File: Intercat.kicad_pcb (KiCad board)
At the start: 2 copper layers, 72 parts, among them U1 CP2615-xx-xM, U10 MAX3250, U11 TLP185, U12 TLP185, U2 USBLC6-2SC6, U3 PCM3060, U4 MCP6002, U5 MCP6002, U6 MCP6002, U8 TLP185, U9 TLP185

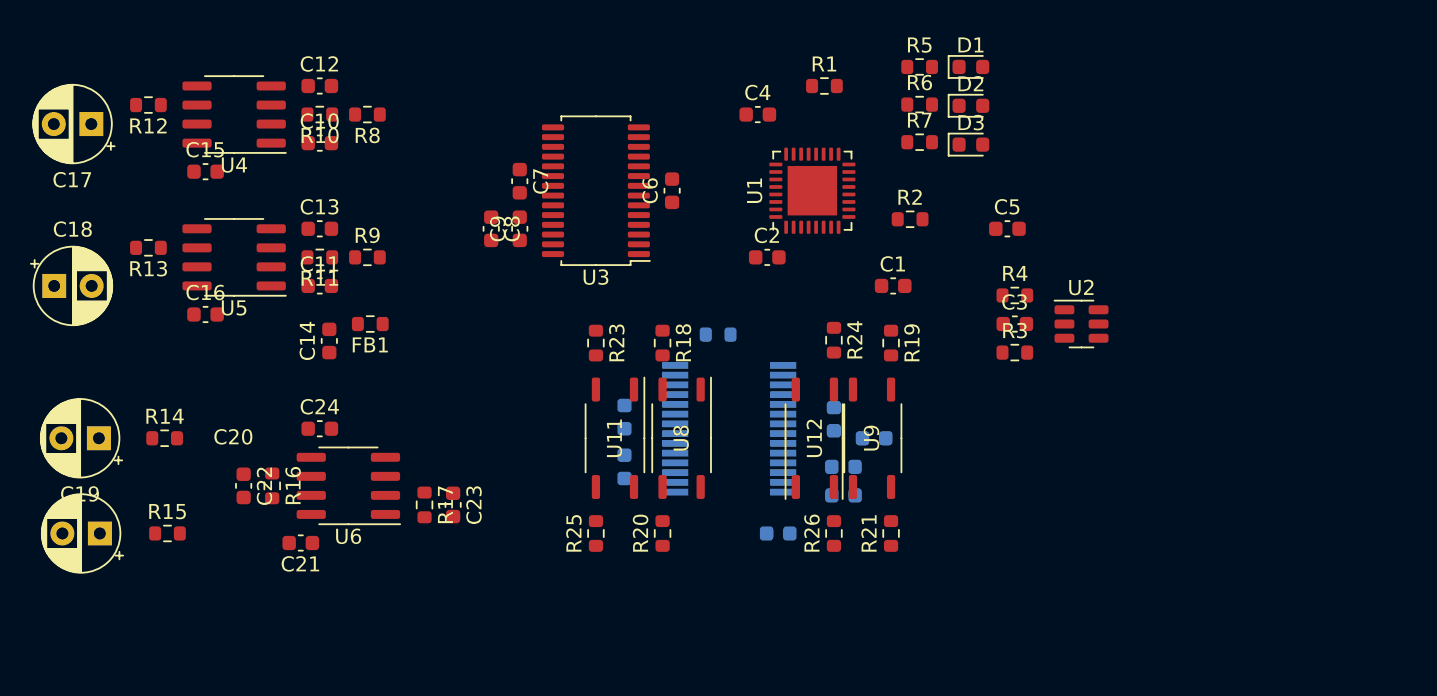
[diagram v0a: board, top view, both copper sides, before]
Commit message: Corrected audio Jacks
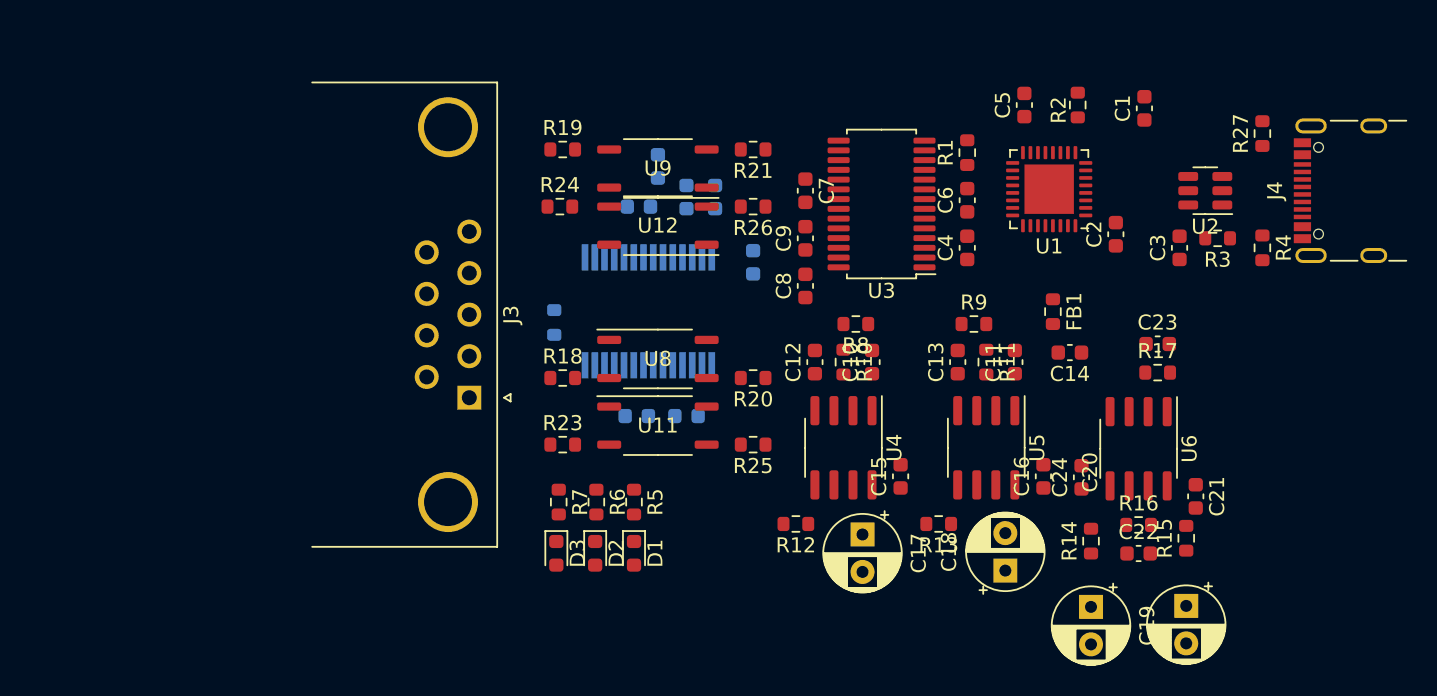
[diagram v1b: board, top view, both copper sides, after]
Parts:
- added J3: DE9_Receptacle, Connector_Dsub:DSUB-9_Female_Horizontal_P2.77x2.84mm_EdgePinOffset7.70mm_Housed_MountingHolesOffset9.12mm, F.Cu at (56.3, 93.2)
- added J4: USB_C_Receptacle_USB2.0, Connector_USB:USB_C_Receptacle_GCT_USB4105-xx-A_16P_TopMnt_Horizontal, F.Cu at (115.6, 79.4)
- added R27: 5k1, Resistor_SMD:R_0603_1608Metric, F.Cu at (109.2, 75.6)
- moved C20 72.6 mm to (104.1, 107.1), turned to -90 degrees
- moved R15 67.9 mm to (104.1, 102.6), turned to 90 degrees
- moved C19 67.1 mm to (97.8, 107.1), turned to -90 degrees
- moved C18 66.2 mm to (92.1, 104.7), turned to 90 degrees
- moved R14 62.2 mm to (97.8, 102.7), turned to 90 degrees
- moved C22 59.9 mm to (101.0, 103.6), turned to 0 degrees
- moved C21 59.8 mm to (104.8, 99.8), turned to -90 degrees
- moved C17 58.3 mm to (82.5, 102.3), turned to -90 degrees
- moved R16 57.8 mm to (101.0, 101.7), turned to 0 degrees
- moved C16 56.9 mm to (94.6, 98.4), turned to 90 degrees
- moved R13 55.8 mm to (87.6, 101.6)
- moved U6 52.8 mm to (101.0, 96.6), turned to -90 degrees
- moved U5 51.7 mm to (90.8, 96.5), turned to -90 degrees
- moved R12 51.4 mm to (78.1, 101.6)
- moved C24 50.9 mm to (97.2, 98.5), turned to 90 degrees
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
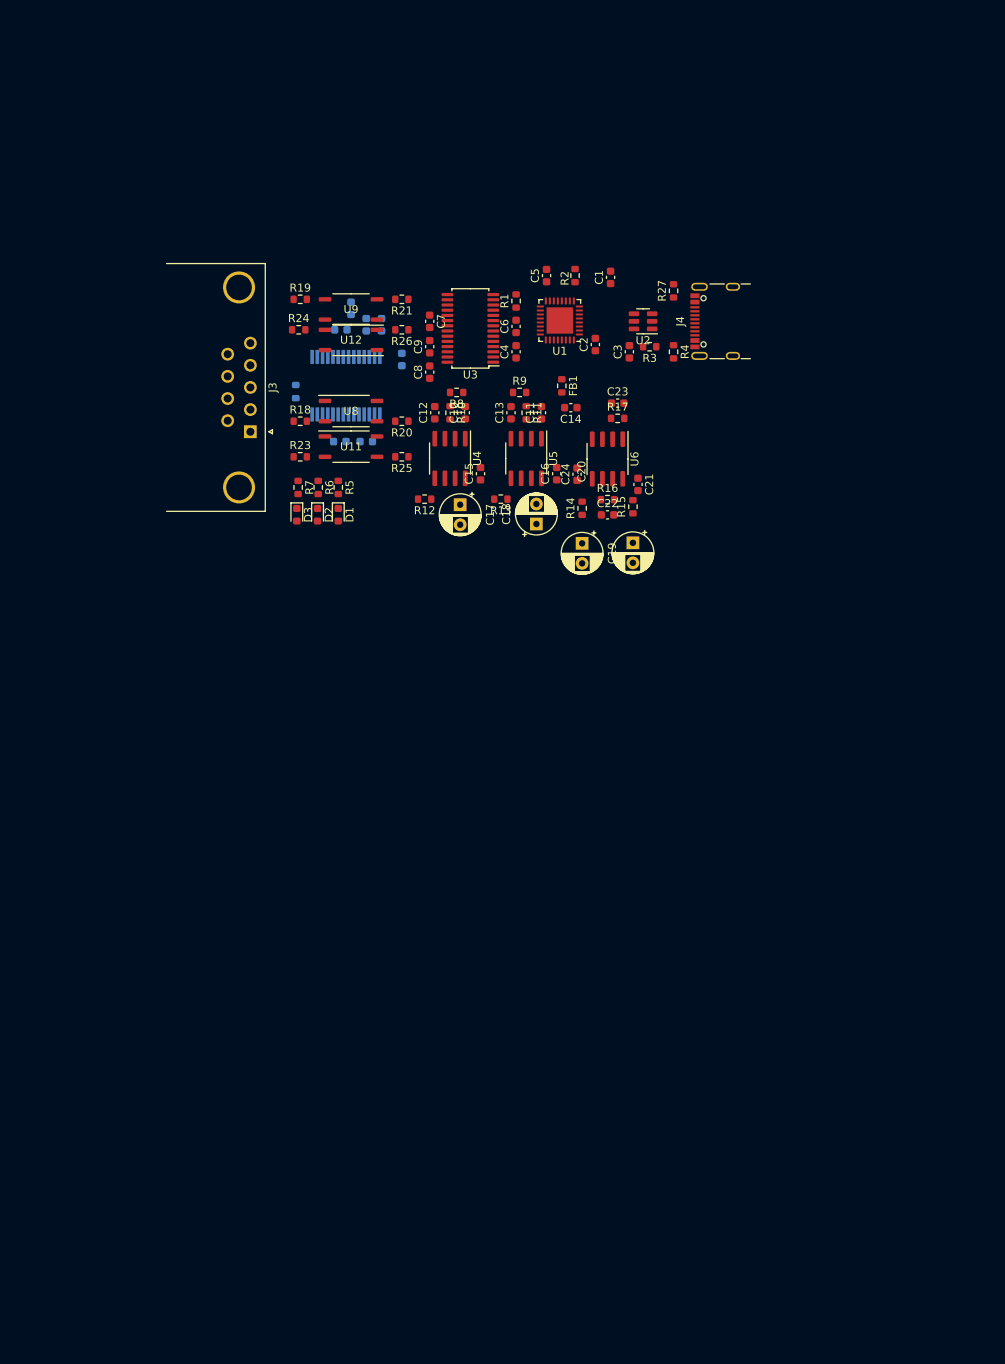
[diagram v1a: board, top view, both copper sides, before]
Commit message: corrected footprint AND symbol of trasf
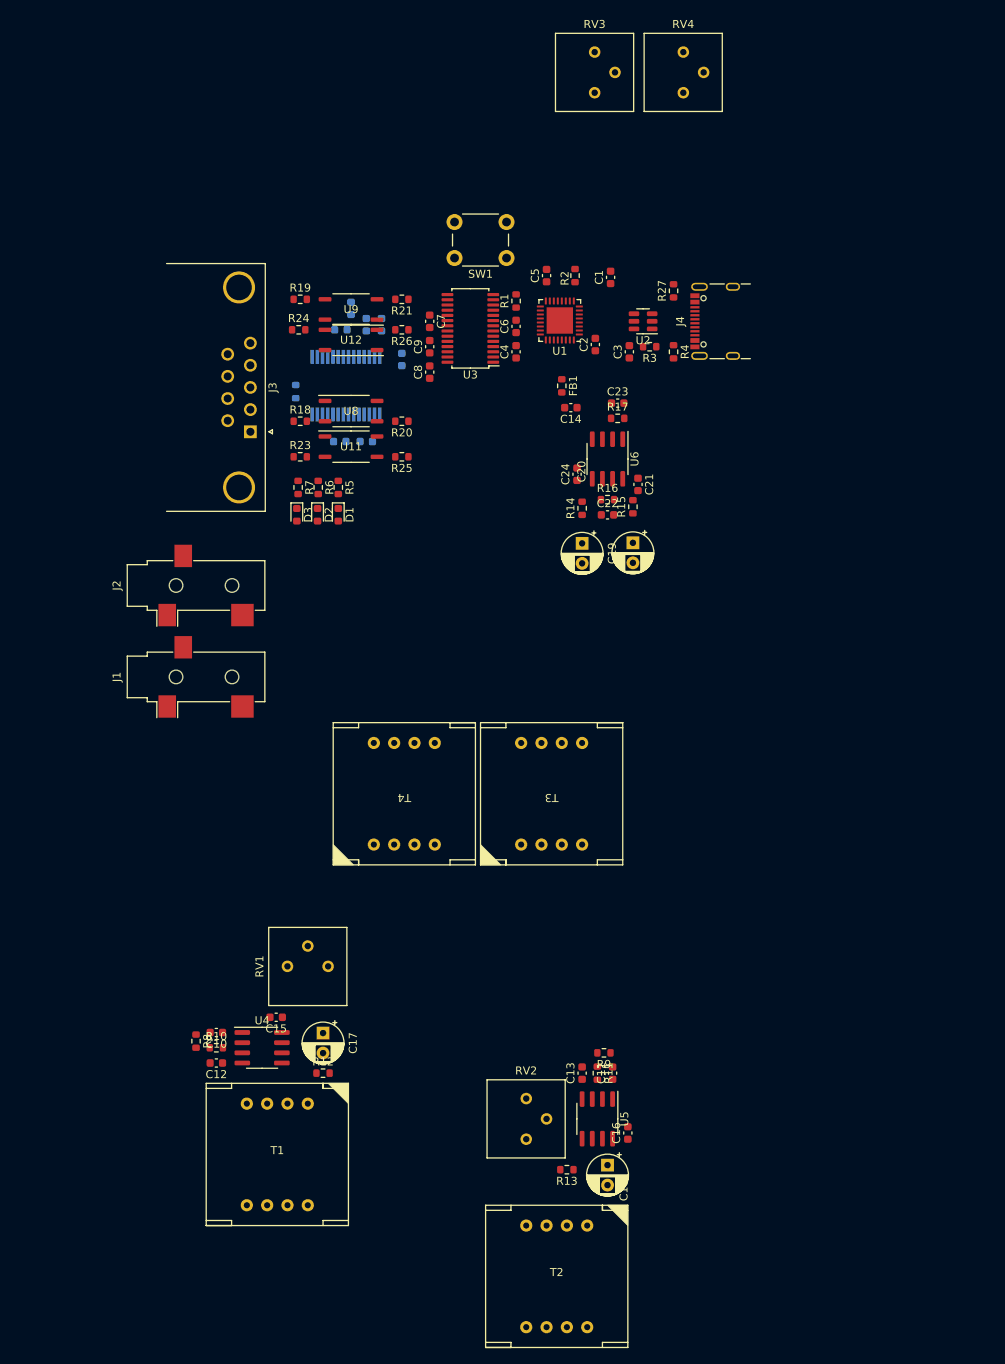
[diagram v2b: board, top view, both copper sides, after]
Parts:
- added J1: AudioJack3, Connector_Audio:Jack_3.5mm_CUI_SJ-3523-SMT_Horizontal, F.Cu at (49.5, 123.8)
- added J2: AudioJack3, Connector_Audio:Jack_3.5mm_CUI_SJ-3523-SMT_Horizontal, F.Cu at (49.5, 112.4)
- added RV1: 10k, Potentiometer_THT:Potentiometer_Bourns_3386P_Vertical, F.Cu at (66.0, 160.0)
- added RV2: 10k, Potentiometer_THT:Potentiometer_Bourns_3386P_Vertical, F.Cu at (90.8, 181.6)
- added RV3: 10k, Potentiometer_THT:Potentiometer_Bourns_3386P_Vertical, F.Cu at (99.4, 50.8)
- added RV4: 10k, Potentiometer_THT:Potentiometer_Bourns_3386P_Vertical, F.Cu at (110.4, 50.8)
- added SW1: SW_Push, Button_Switch_THT:SW_PUSH_6mm, F.Cu at (88.3, 71.5)
- added T1: LM-NP-1001-B1L, InterCat:LM-NP-1001-B1L, F.Cu at (59.7, 183.5)
- added T2: LM-NP-1001-B1L, InterCat:LM-NP-1001-B1L, F.Cu at (94.6, 198.8)
- added T3: LM-NP-1001-B1L, InterCat:LM-NP-1001-B1L, F.Cu at (94.0, 138.4)
- added T4: LM-NP-1001-B1L, InterCat:LM-NP-1001-B1L, F.Cu at (75.6, 138.4)
- moved R8 87.4 mm to (49.5, 169.4), turned to -90 degrees
- moved C12 85.7 mm to (52.1, 172.1), turned to 180 degrees
- moved R10 84.6 mm to (52.1, 170.2), turned to 0 degrees
- moved R13 84.2 mm to (95.9, 185.4)
- moved C10 83.5 mm to (52.1, 168.3), turned to 180 degrees
- moved R9 83.2 mm to (100.5, 170.8), turned to 180 degrees
- moved U5 83.0 mm to (99.7, 179.1)
- moved C11 83.0 mm to (101.6, 173.4)
- moved C13 83.0 mm to (97.8, 173.4)
- moved R11 83.0 mm to (99.7, 173.4)
- moved C16 82.9 mm to (103.5, 180.8)
- moved C18 80.6 mm to (101.0, 184.8), turned to -90 degrees
- moved U4 77.3 mm to (57.8, 170.2), turned to 0 degrees
- moved R12 72.9 mm to (65.4, 173.4), turned to 0 degrees
- moved C15 72.6 mm to (59.5, 166.4), turned to 180 degrees
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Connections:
- J3 pad 1: GND -> GNDA
- J3 pad 5: GND -> GNDA
- J3 pad 6: VBUS -> VS
- U11 pad 6: VBUS -> VS
- U8 pad 6: VBUS -> VS

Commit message: first PCB placement Draft
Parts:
- moved RV3 87.0 mm to (143.5, 125.7)
- moved D1 79.2 mm to (146.0, 112.6)
- moved D2 79.2 mm to (143.4, 112.6)
- moved D3 79.2 mm to (140.8, 112.6)
- moved R5 79.2 mm to (146.0, 109.2)
- moved R7 79.2 mm to (141.0, 109.2)
- moved R6 79.2 mm to (143.5, 109.2)
- moved RV4 75.2 mm to (116.8, 125.7)
- moved R8 69.2 mm to (85.9, 110.5), turned to 180 degrees
- moved C12 66.7 mm to (83.2, 113.0), turned to 90 degrees
- moved R10 66.0 mm to (85.1, 113.0), turned to -90 degrees
- moved C10 65.4 mm to (87.0, 113.0), turned to 90 degrees
- moved R13 62.1 mm to (104.1, 123.8)
- moved T2 61.3 mm to (101.0, 137.8)
- moved C18 60.8 mm to (108.6, 124.5)
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
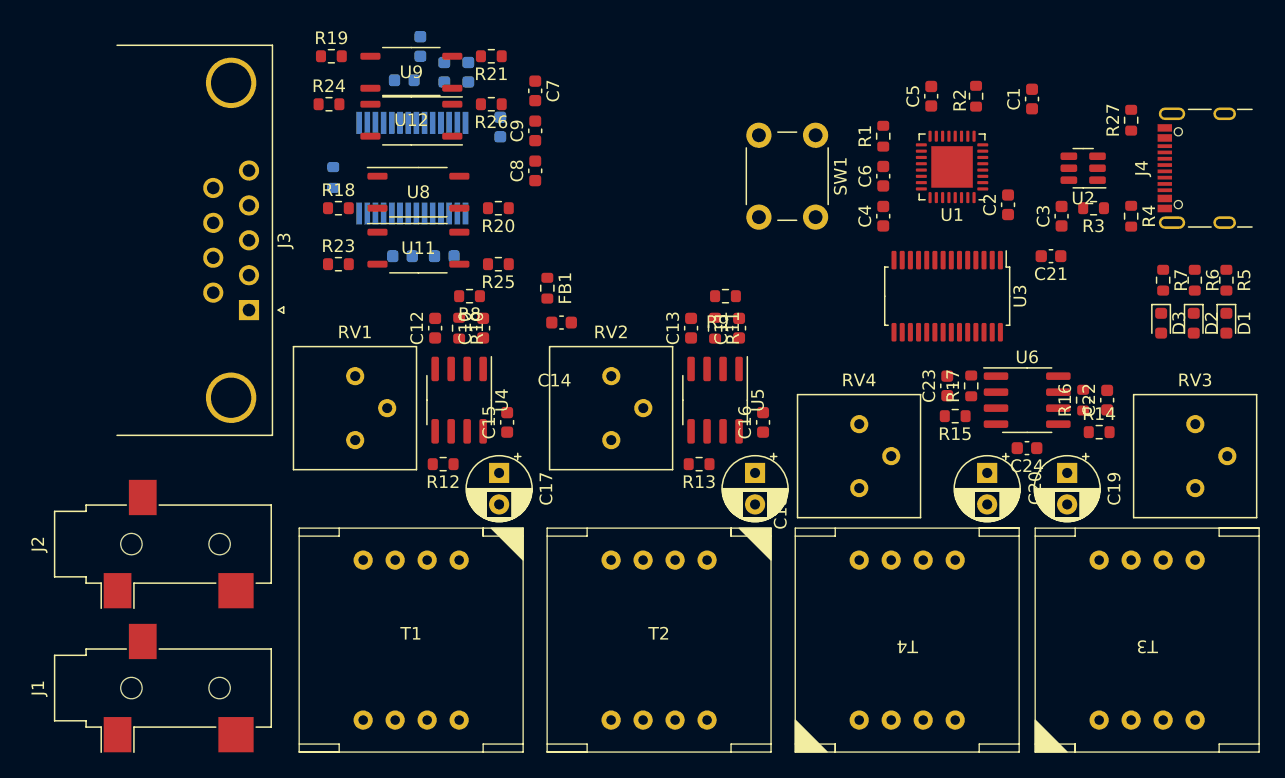
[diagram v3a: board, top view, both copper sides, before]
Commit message: removed jack connectors, added testpoints on DAC
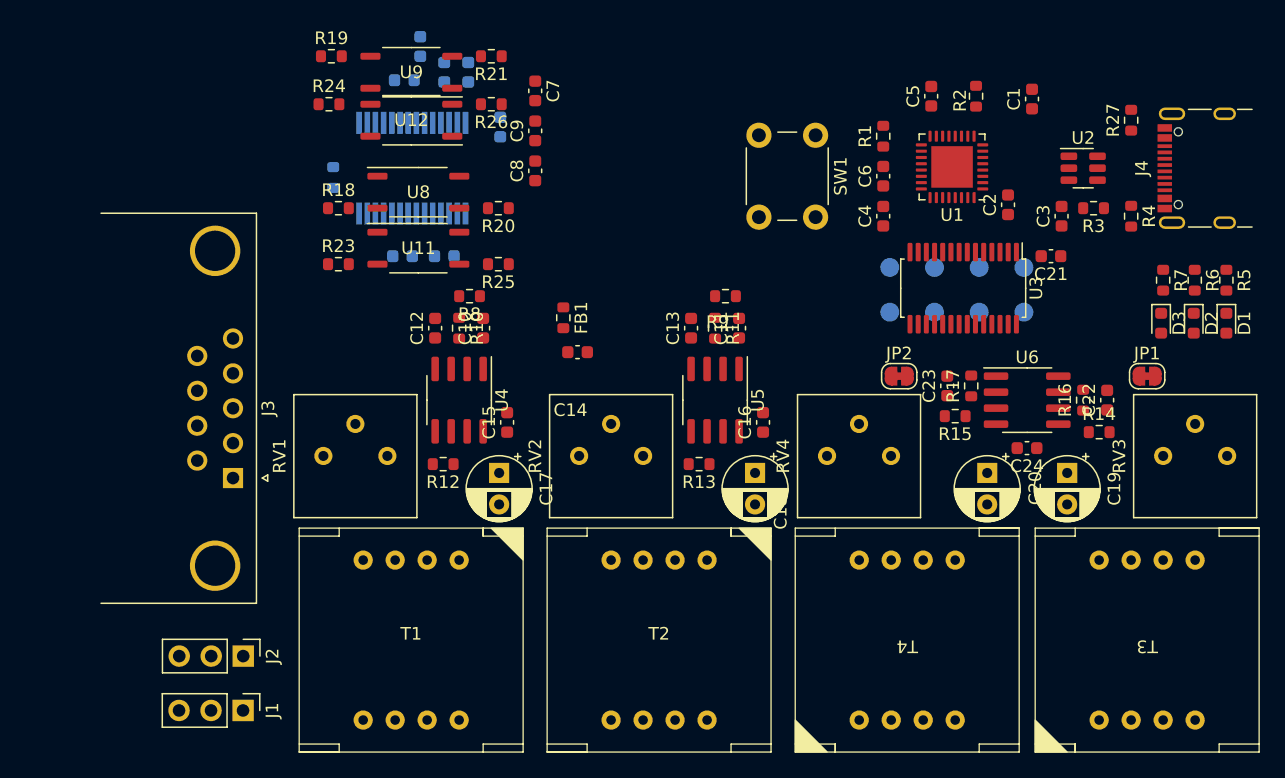
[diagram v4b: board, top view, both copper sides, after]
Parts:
- added JP1: Jumper_2_Bridged, Jumper:SolderJumper-2_P1.3mm_Bridged_RoundedPad1.0x1.5mm, F.Cu at (139.7, 116.8)
- added JP2: Jumper_2_Bridged, Jumper:SolderJumper-2_P1.3mm_Bridged_RoundedPad1.0x1.5mm, F.Cu at (120.0, 116.8)
- added TP1: TestPoint, TestPoint:TestPoint_Pad_D1.5mm, B.Cu at (129.9, 108.2)
- added TP2: TestPoint, TestPoint:TestPoint_Pad_D1.5mm, B.Cu at (129.9, 111.8)
- added TP3: TestPoint, TestPoint:TestPoint_Pad_D1.5mm, B.Cu at (126.4, 108.2)
- added TP4: TestPoint, TestPoint:TestPoint_Pad_D1.5mm, B.Cu at (126.4, 111.8)
- added TP5: TestPoint, TestPoint:TestPoint_Pad_D1.5mm, B.Cu at (122.8, 108.2)
- added TP6: TestPoint, TestPoint:TestPoint_Pad_D1.5mm, B.Cu at (122.8, 111.8)
- added TP7: TestPoint, TestPoint:TestPoint_Pad_D1.5mm, B.Cu at (119.3, 108.2)
- added TP8: TestPoint, TestPoint:TestPoint_Pad_D1.5mm, B.Cu at (119.3, 111.8)
- J1, J2: value AudioJack3 -> Conn_01x03; footprint Connector_Audio:Jack_3.5mm_CUI_SJ-3523-SMT_Horizontal -> Connector_PinHeader_2.54mm:PinHeader_1x03_P2.54mm_Vertical
- moved J3 13.4 mm to (67.1, 124.9)
- moved J2 10.9 mm to (67.9, 139.1), turned to -90 degrees
- moved J1 6.60 mm to (67.9, 143.4), turned to -90 degrees
- moved RV3 3.59 mm to (146.1, 123.2), turned to 90 degrees
- moved RV4 3.59 mm to (119.4, 123.2), turned to 90 degrees
- moved RV1 2.85 mm to (79.4, 123.2), turned to 90 degrees
- moved RV2 2.82 mm to (99.7, 123.2), turned to 90 degrees
- moved C14 2.67 mm to (94.5, 114.9)
- moved FB1 2.67 mm to (93.3, 112.2)
- moved U3 1.42 mm to (125.1, 109.9)
- turned U2 to 0 degrees
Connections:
- C22 pad 2: /ADC_Lin -> Net-(JP1-A)
- C23 pad 2: /ADC_Rin -> Net-(JP2-A)
- R16 pad 2: /ADC_Lin -> Net-(JP1-A)
- R17 pad 2: /ADC_Rin -> Net-(JP2-A)
- U3 pad 13: unconnected-(U3-ZEROR-Pad13) -> Net-(U3-ZEROR)
- U3 pad 14: unconnected-(U3-ZEROL-Pad14) -> Net-(U3-ZEROL)
- U3 pad 17: unconnected-(U3-Vout_R--Pad17) -> Net-(U3-Vout_R-)
- U3 pad 19: unconnected-(U3-Vout_L--Pad19) -> Net-(U3-Vout_L-)
- U6 pad 1: /ADC_Rin -> Net-(JP2-A)
- U6 pad 7: /ADC_Lin -> Net-(JP1-A)
